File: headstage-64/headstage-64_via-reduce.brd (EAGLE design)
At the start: 23.4 x 25.8 mm, 183 parts, among them J8 DF40C-70DP-0.4V(51), J9 PINHD-1X5_HALF_CONNETOR, U1 CAT4016_QFN, U10 TS4231, U11 DS90UB913A_WQFN, U12 TS4231, U13 TS4231, U14 TLV70733, U15 10M08DC, U16 TLV70733, U17 LT3463, U18 TLV70725, U19 TPS62621, U2 OPA170, U20 ASCO-50.000MHZ-EK-T3, U21 TLV70712, U3 INA826, U4 DAC5311, U5 TPL0501_UQFN, U6 DG509B, U7 TS4231, U8 MPU9250_QFN_NO-PAD, U9 RHD2064_BGA

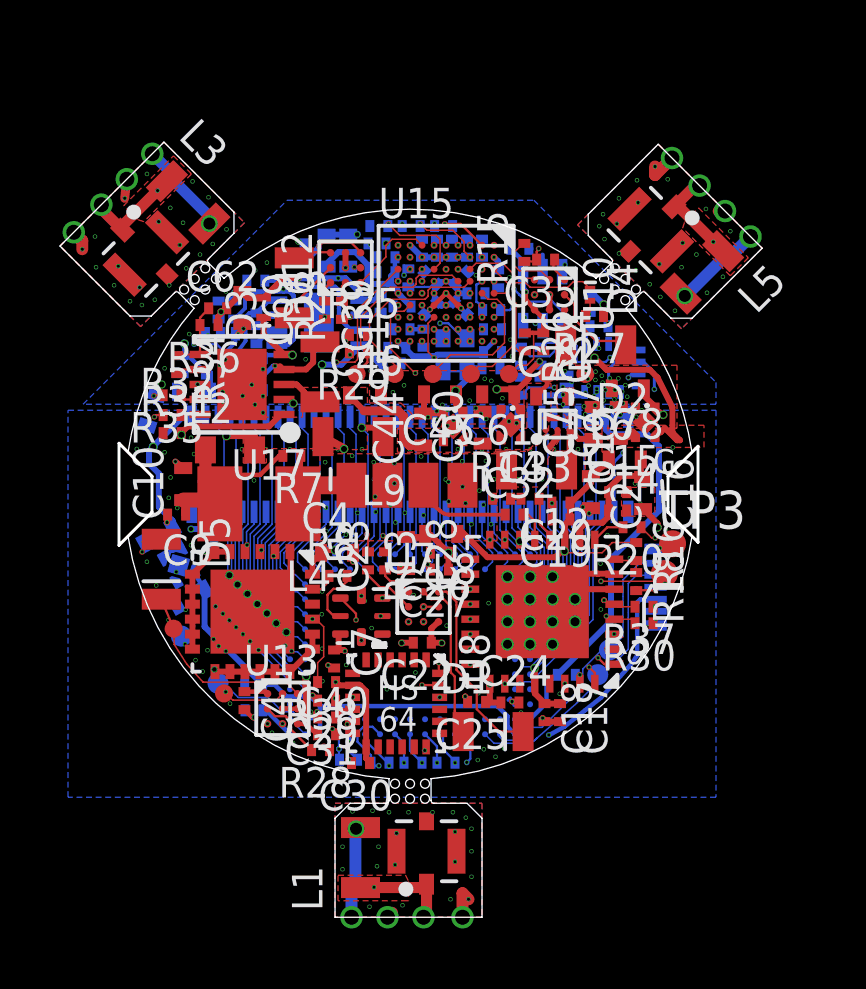
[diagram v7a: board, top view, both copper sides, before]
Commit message: Added ESD protection to host board and headstages
- Host board has a high-voltage RC circuit between isolaed ground planes
to prevent common-mode voltage accumulation on isolated side
- TVS diodes are installed on headstage and host board sides to take
care of ESD events.
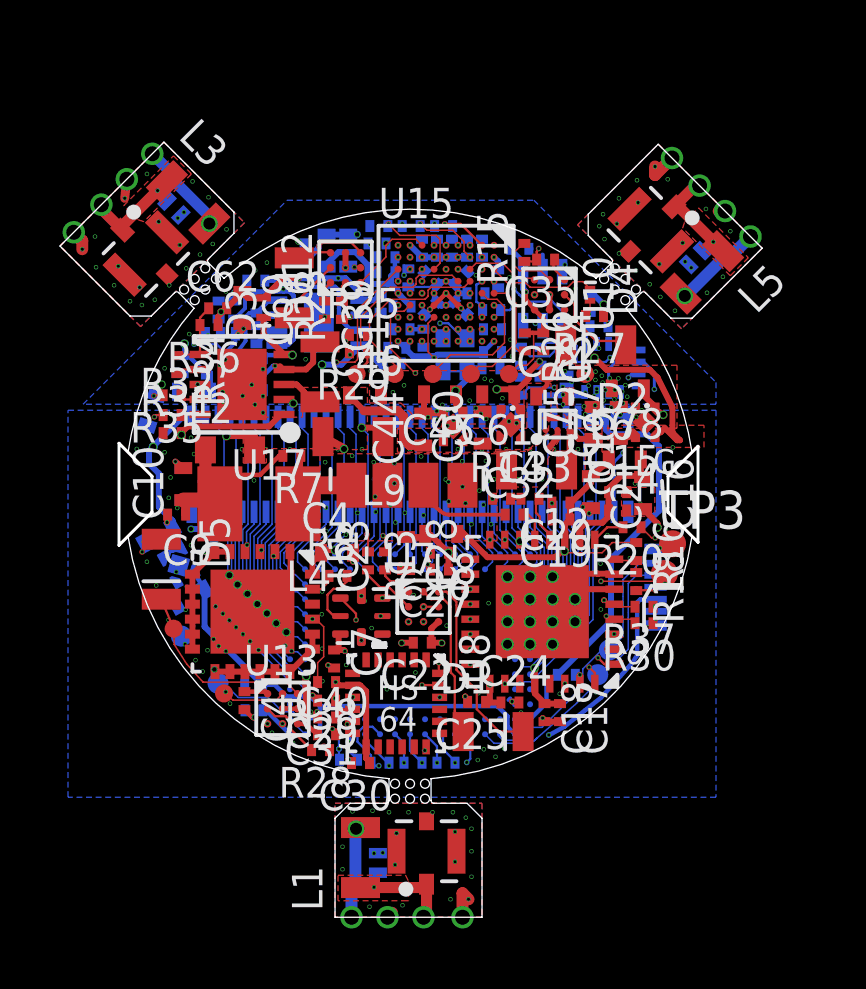
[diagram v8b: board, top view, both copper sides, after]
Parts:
- added D7, D8, D9: SESD0402X1UN-0020-090, jonnew:0402T-DFN
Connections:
- net GND1: now also D8.A
- net GND2: now also D7.A
- net GND3: now also D9.A
- net _SIGOUT: now also D8.C
- net _SIGOUT1: now also D7.C
- net _SIGOUT2: now also D9.C
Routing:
- net _SIGOUT1: track 3.76 -> 4.31 mm
- net _SIGOUT2: track 3.76 -> 4.26 mm
- removed copper zone on layer 4, net N$47
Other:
- board text added: "HS-64 JPN JV"
- board text removed: "HS 64 JPN&JV"
